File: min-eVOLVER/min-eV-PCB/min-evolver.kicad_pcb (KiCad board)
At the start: 4 copper layers, 109.2 x 64.5 mm, 72 parts, among them CON1 BARREL_JACK, P1 CONN_02X12, P2 CONN_02X08, P3 CONN_02X08, P4 CONN_02X08, P7 , Q1 Q_NMOS_GSD, Q10 Q_NMOS_GSD, Q11 Q_NMOS_GSD, Q12 Q_NMOS_GSD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

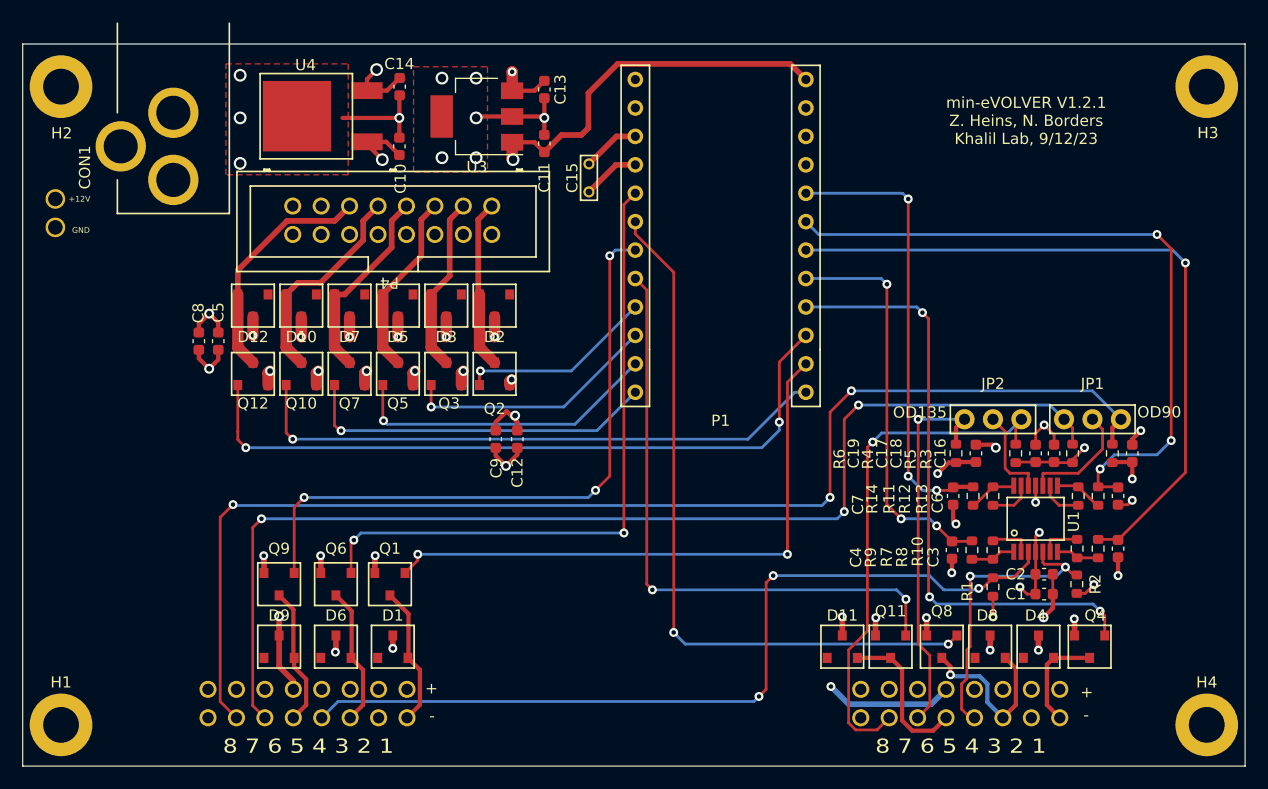
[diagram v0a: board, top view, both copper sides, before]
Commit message: min-eV PCBv1.2.2 better diode and mosfet footprints, corrected PCBway BOM (OD90 and OD135 resistors were swapped)
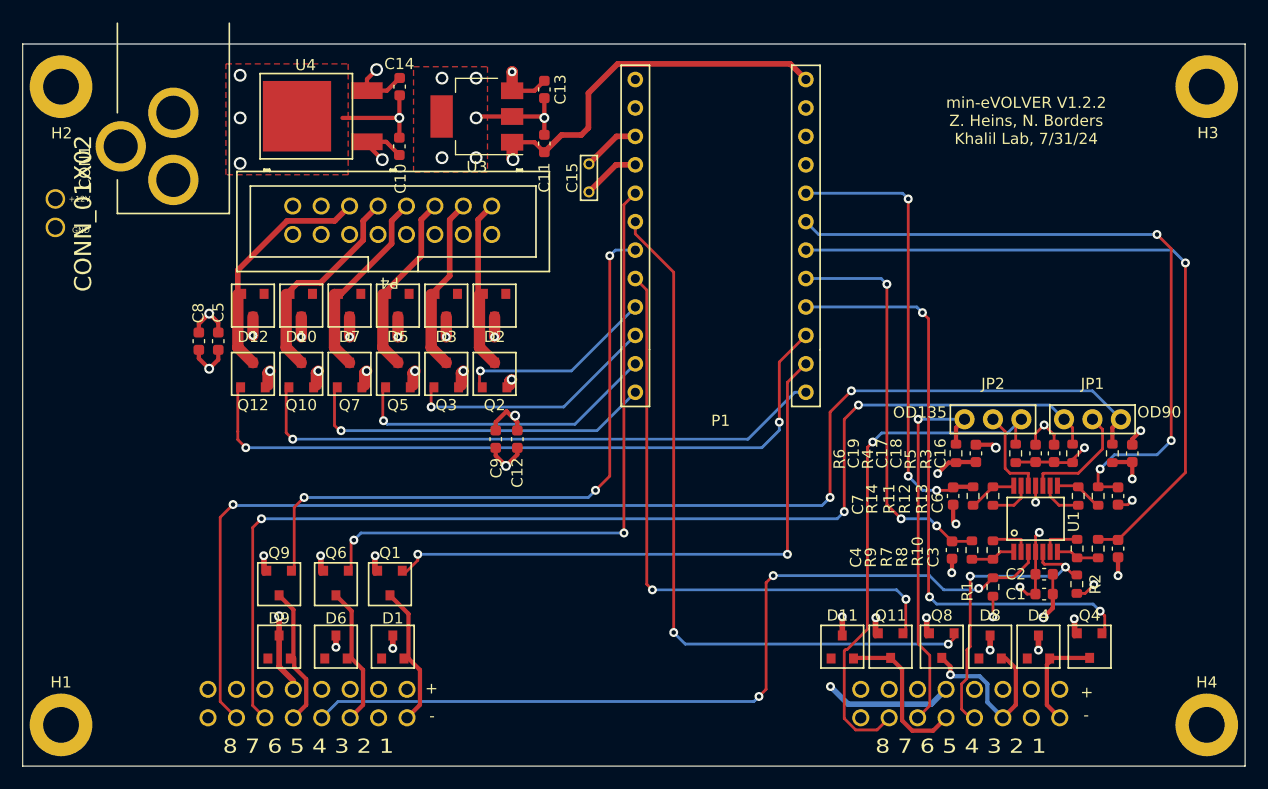
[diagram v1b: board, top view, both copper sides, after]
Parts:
- D1, D10, D11, D12, D2, D3, D4, D5, D6, D7, D8, D9: footprint mods:SBR160S23 -> min-eV-footprint-lib:diode_SBR160S23
- P7: value (none) -> CONN_01X02
- Q1, Q10, Q11, Q12, Q2, Q3, Q4, Q5, Q6, Q7, Q8, Q9: footprint mods:A03422 -> min-eV-footprint-lib:mosfet_A03422
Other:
- board text added: "min-eVOLVER V1.2.2 Z. Heins, N. Borders Khalil Lab, 7/31/24"
- board text removed: "min-eVOLVER V1.2.1 Z. Heins, N. Borders Khalil Lab, 9/12/23"
